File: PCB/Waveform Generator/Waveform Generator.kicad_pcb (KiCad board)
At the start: 4 copper layers, 80 x 104.1 mm, 141 parts, among them J1 Power input, J10 USART1_2, J12 Signal 2, J19 ADC_2, J2 RS485_1, J20 TIMER_1, J21 I2C1_1, J22 TIMER_2, J23 I2C1_2, J3 USB_B_Micro, J5 Signal 1, J6 SWD, J7 RS485_2, J8 USART1_1, J9 ADC_1, Q0 AO3401A, Q1 Q_NPN_BCE, Q2 Q_NPN_BCE, Q3 Q_PNP_BCE, Q4 Q_NPN_BCE, Q5 Q_NPN_BCE, Q6 Q_NPN_BCE, Q7 Q_NPN_BCE, Q8 Q_NPN_BCE, SW1 SW_SPDT, SW2 SW_SPDT, SW3 SW_SPDT, T0 5001, T1 5001, T2 5001, T3 5001, T4 5001, T5 5001, T6 5001, T7 5001, U1 STM32F427VITx, U10 USBLC6-2SC6, U11 USBLC6-2SC6, U2 MAX485EESAT, U3 USBLC6-2SC6, U4 OPA1602, U5 OPA1602, U6 USBLC6-2SC6, U7 USBLC6-2SC6, U8 LM335ADT, U9 USBLC6-2SC6, X1 25MHZ

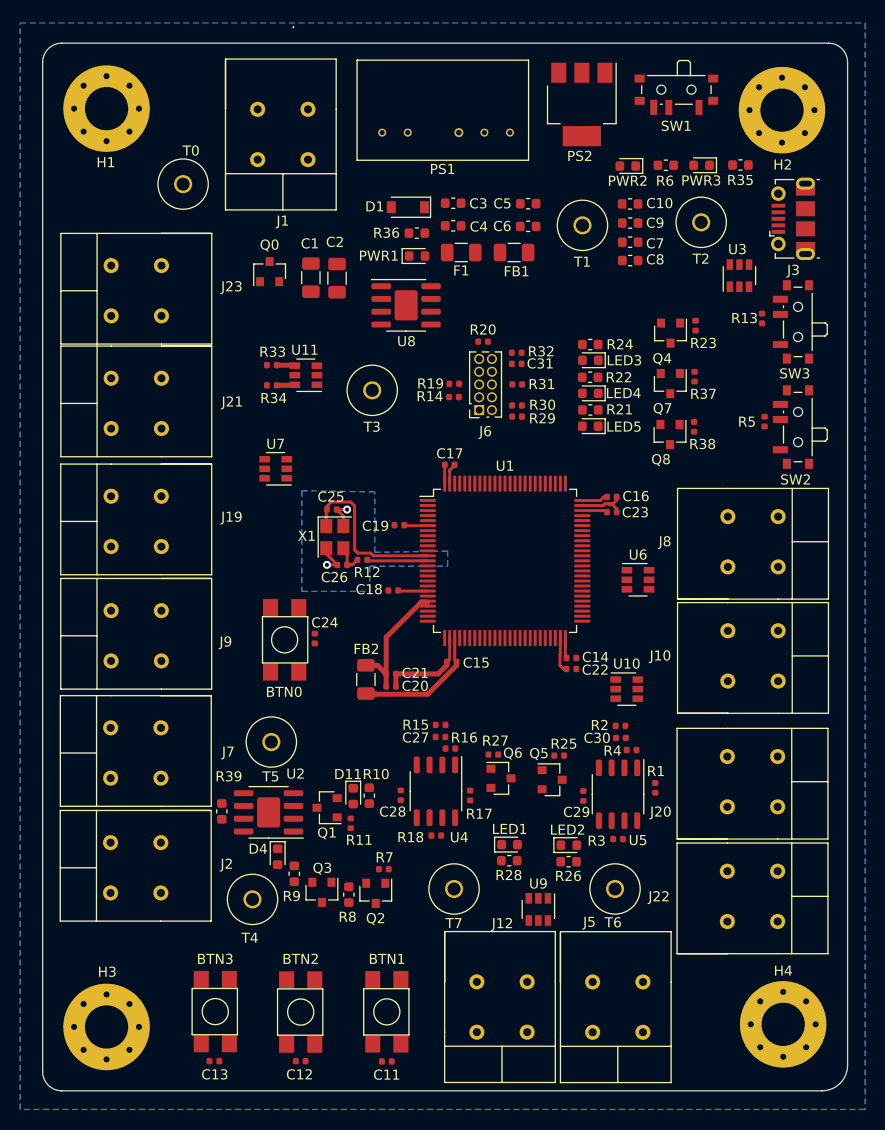
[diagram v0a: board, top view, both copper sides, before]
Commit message: Routing power
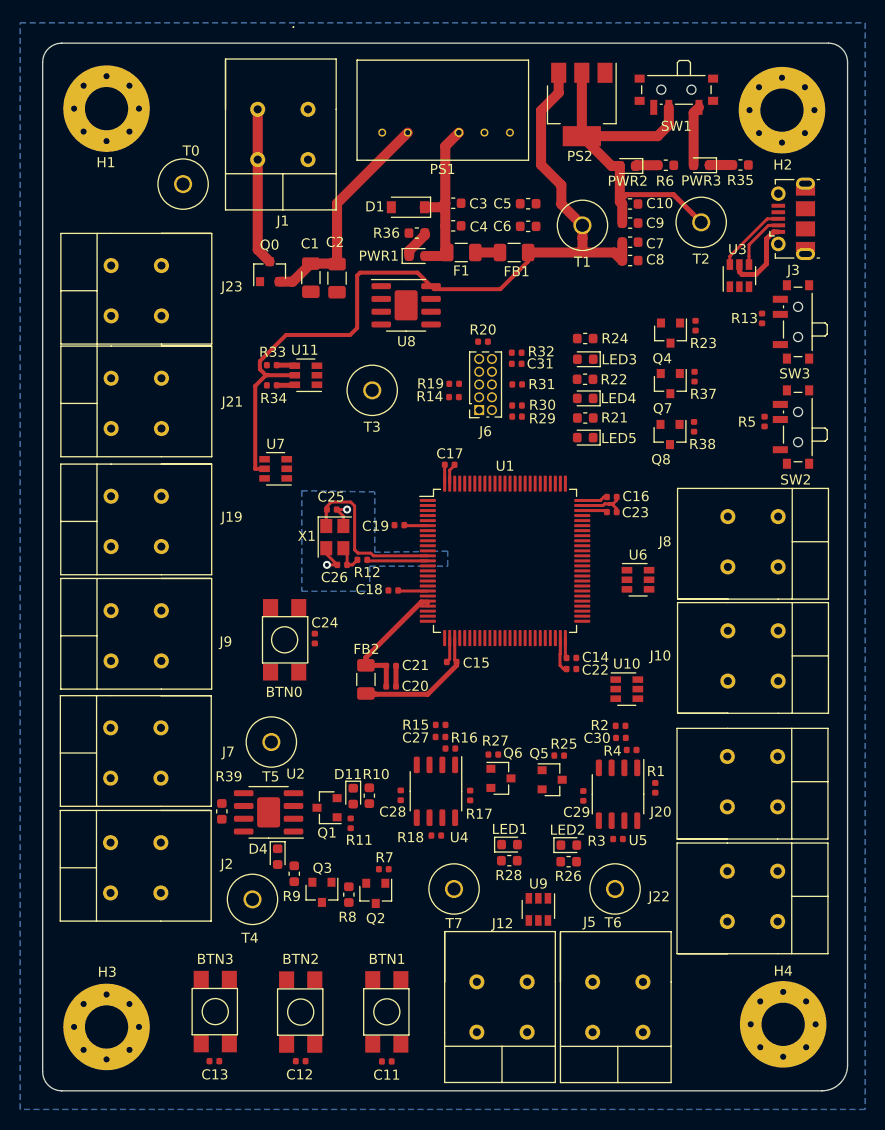
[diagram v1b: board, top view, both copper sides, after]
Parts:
- moved LED5 1.24 mm to (69.2, 48.1)
- moved R21 0.94 mm to (69.2, 46.1)
- moved C21 0.79 mm to (49.9, 70.8)
- moved R24 0.78 mm to (69.2, 38.2)
- moved LED4 0.71 mm to (69.2, 44.2)
- moved R22 0.54 mm to (69.2, 42.3)
- moved LED3 0.51 mm to (69.2, 40.3)
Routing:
- net +5V: track 0.00 -> 83.0 mm
- net Net-(C10-Pad1): track 0.00 -> 37.6 mm
- net Net-(C1-Pad1): track 0.00 -> 22.5 mm
- net Net-(C3-Pad1): track 0.00 -> 17.1 mm
- net VCC: track 0.00 -> 15.6 mm
- net VBUS: track 0.00 -> 7.89 mm
- net Net-(J3-Pad3): track 0.00 -> 7.19 mm
- net +3V3: track 24.9 -> 30.9 mm
- net Net-(J3-Pad2): track 0.00 -> 5.68 mm
- net GND: track 27.0 -> 22.0 mm
- net Net-(PWR1-Pad1): track 0.00 -> 2.92 mm
- net Net-(F1-Pad1): track 0.00 -> 2.45 mm
- net Net-(PWR3-Pad1): track 0.00 -> 2.30 mm
- net Net-(PWR2-Pad1): track 0.00 -> 2.24 mm

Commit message: Working on PCB tracks
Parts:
- moved Q7 5.30 mm to (77.7, 48.0)
- moved R37 5.27 mm to (80.3, 47.3)
- moved R38 5.04 mm to (80.2, 42.0)
- moved Q8 4.99 mm to (77.7, 42.8)
- moved U6 1.83 mm to (74.9, 64.0)
- moved T3 1.57 mm to (48.7, 42.0)
- moved C15 1.06 mm to (55.2, 71.2)
- moved H3 0.18 mm to (21.6, 106.5)
- moved J8 0.07 mm to (83.2, 58.4)
- turned LED2 to 180 degrees
- turned R31 to 180 degrees
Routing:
- net BTN3_Input: track 0.00 -> 69.0 mm, vias 0 -> 2
- net BTN2_Input: track 0.00 -> 65.7 mm, vias 0 -> 2
- net BTN1_Input: track 0.00 -> 58.2 mm, vias 0 -> 2
- net +5V: track 83.0 -> 33.7 mm, vias 0 -> 1
- net MAX485_PWR: track 0.00 -> 38.8 mm, vias 0 -> 2
- net ADC2_IN0: track 0.00 -> 33.0 mm, vias 0 -> 2
- net LED3: track 0.00 -> 31.5 mm
- net NRST: track 0.00 -> 28.9 mm
- net ADC1_IN1: track 0.00 -> 27.9 mm, vias 0 -> 2
- net USART2_RX: track 0.00 -> 27.1 mm, vias 0 -> 2
- net Net-(J7-Pad1): track 0.00 -> 26.8 mm
- net Net-(J22-Pad1): track 0.00 -> 26.4 mm
- net LED1: track 0.00 -> 25.6 mm, vias 0 -> 2
- net LED4: track 0.00 -> 25.4 mm
- net Net-(J2-Pad2): track 0.00 -> 23.4 mm
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- removed copper zone on In2.Cu, net +3V3
- removed copper zone on B.Cu, net GND

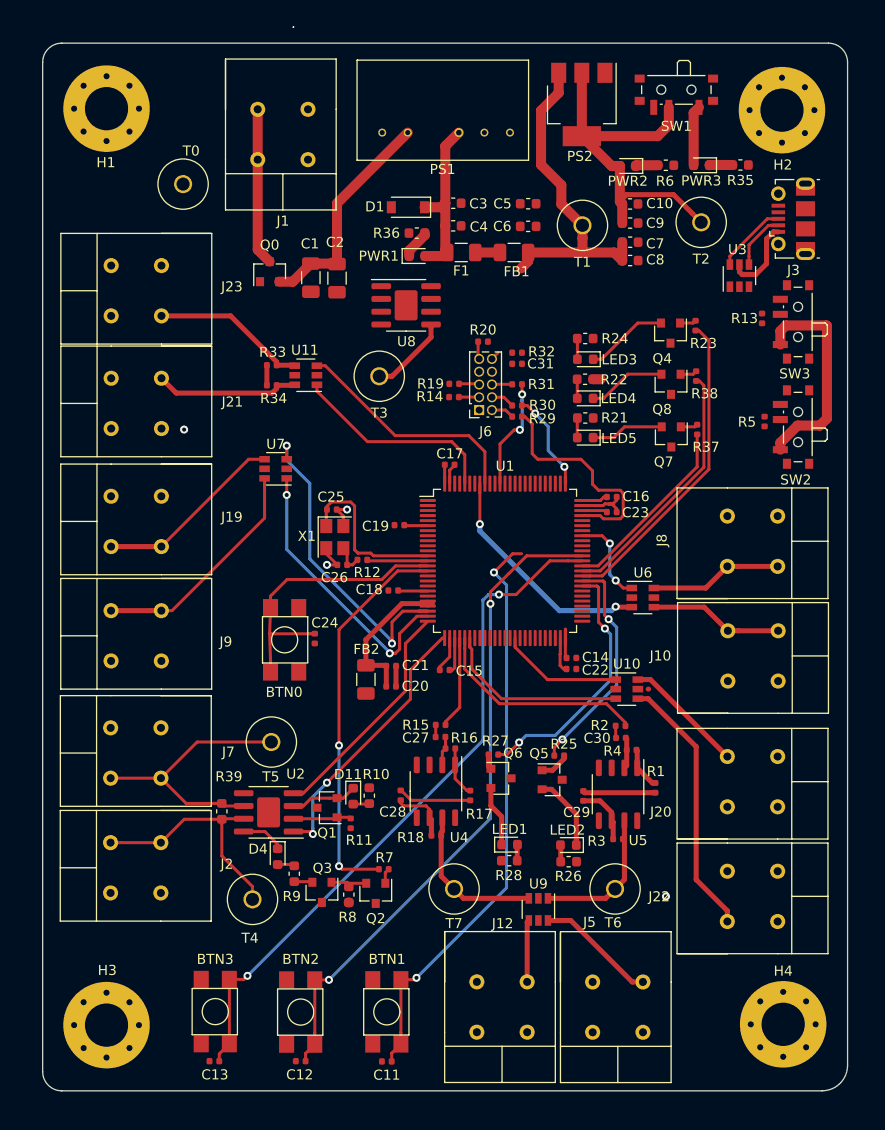
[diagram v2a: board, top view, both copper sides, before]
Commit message: Busy with ground planes
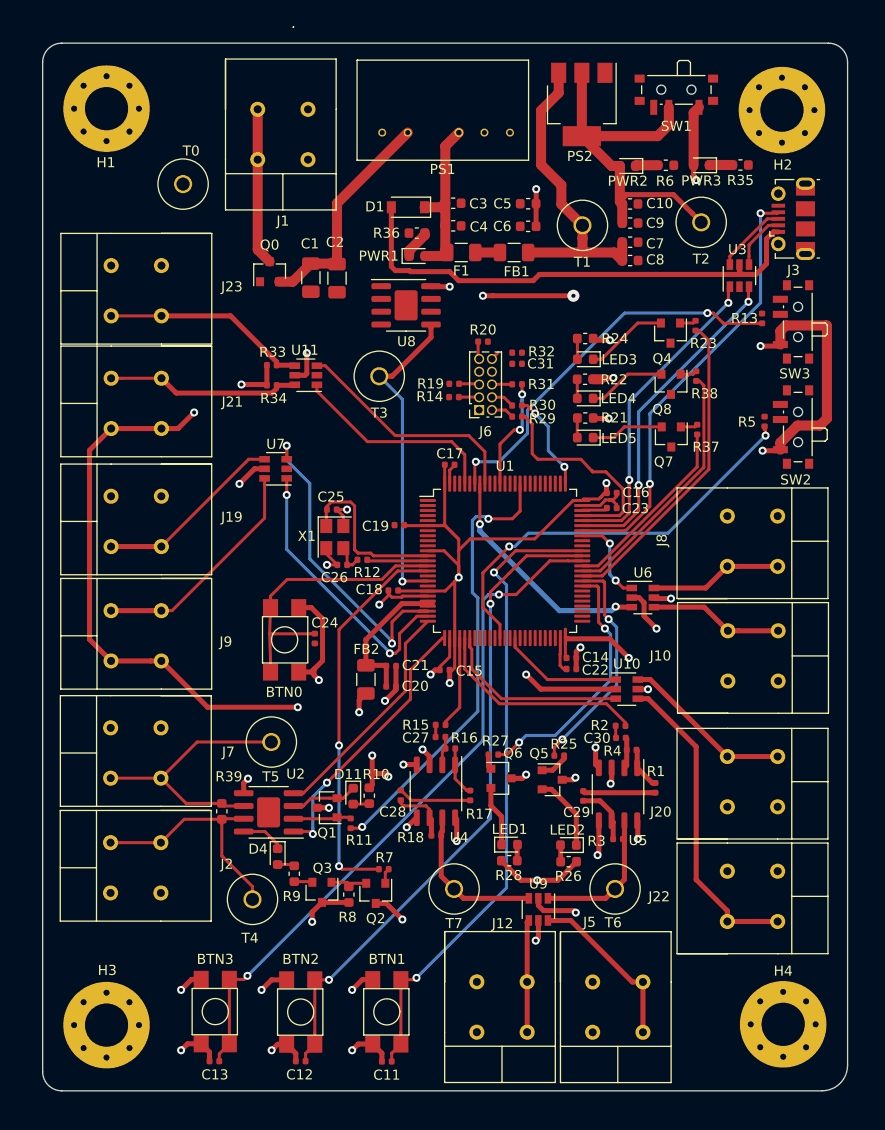
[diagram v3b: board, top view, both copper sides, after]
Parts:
- moved C16 0.40 mm to (71.8, 53.6)
- moved C23 0.40 mm to (71.8, 55.1)
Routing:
- net +3V3: track 46.9 -> 482.6 mm, vias 1 -> 19
- net +5V: track 33.7 -> 238.2 mm, vias 1 -> 9
- net -5V: track 0.00 -> 128.0 mm, vias 0 -> 3
- net GND: track 23.1 -> 102.4 mm, vias 2 -> 25
- net USART2_RTS: track 0.00 -> 44.7 mm, vias 0 -> 2
- net USB_ID: track 0.00 -> 43.2 mm, vias 0 -> 2
- net VBUS: track 7.89 -> 50.1 mm
- net BOOT1: track 0.00 -> 42.0 mm, vias 0 -> 2
- net BOOT0: track 0.00 -> 38.6 mm, vias 0 -> 2
- net USB_D-: track 0.00 -> 33.0 mm, vias 0 -> 2
- net USB_D+: track 0.00 -> 32.5 mm, vias 0 -> 2
- net TEMP_SENSE: track 8.02 -> 31.9 mm, vias 0 -> 1
- net BTN1_Input: track 58.2 -> 64.4 mm
- net Net-(J5-Pad1): track 12.0 -> 17.0 mm
- net Net-(J21-Pad2): track 14.4 -> 19.4 mm
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- added copper zone on In2.Cu, net +3V3

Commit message: Benchmark, looks if the majority of the work is complete
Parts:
- moved C23 1.62 mm to (71.0, 53.7)
- moved C16 1.29 mm to (71.0, 52.6)
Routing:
- net GND: track 102.4 -> 190.5 mm, vias 25 -> 49
- net NRST: track 28.9 -> 62.1 mm, vias 0 -> 2
- net +3V3: track 482.6 -> 478.9 mm, vias 19 -> 18
- net Net-(LED4-Pad1): track 7.69 -> 10.3 mm
- net Net-(LED3-Pad1): track 8.22 -> 10.3 mm
- net Net-(R5-Pad1): track 0.00 -> 1.69 mm
- net Net-(J6-Pad10): track 0.88 -> 2.27 mm
- net SWDIO: track 22.2 -> 22.7 mm

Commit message: Monday morning grind
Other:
- board text added: "Waveform Generator V1 Nanodyn Systems"
- board text removed: "Waveform Generator v1 Nanodyn Systems"
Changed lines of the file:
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@@
     (32 B.Adhes user)
     (33 F.Adhes user)
-    (34 B.Paste user)
+    (34 B.Paste user hide)
     (35 F.Paste user)
     (36 B.SilkS user)
@@
     (tags capacitor)
     (attr smd)
-    (fp_text reference C1 (at -3.37 0.09 180) (layer F.SilkS)
+    (fp_text reference C1 (at -3 0 180) (layer F.SilkS)
       (effects (font (size 1 1) (thickness 0.15)))
     )
@@
     (tags capacitor)
     (attr smd)
-    (fp_text reference C2 (at 3.57 -0.19 180) (layer F.SilkS)
+    (fp_text reference C2 (at 3.05 0 180) (layer F.SilkS)
       (effects (font (size 1 1) (thickness 0.15)))
     )
@@
     (tags capacitor)
     (attr smd)
-    (fp_text reference C31 (at -2.35 0) (layer F.SilkS)
+    (fp_text reference C31 (at -2.4 -0.04) (layer F.SilkS)
       (effects (font (size 1 1) (thickness 0.15)))
     )
@@
     (tags SOT-23)
     (attr smd)
-    (fp_text reference Q0 (at 2.65 0 180) (layer F.SilkS)
+    (fp_text reference Q0 (at 2.5 0.1 180) (layer F.SilkS)
       (effects (font (size 1 1) (thickness 0.15)))
     )
@@
     (tags resistor)
     (attr smd)
-    (fp_text reference R13 (at 0 1.75 180) (layer F.SilkS)
+    (fp_text reference R13 (at 0.05 1.95 180) (layer F.SilkS)
       (effects (font (size 1 1) (thickness 0.15)))
     )
@@
     (tags resistor)
     (attr smd)
-    (fp_text reference R31 (at -2.415 0) (layer F.SilkS)
+    (fp_text reference R31 (at -2.5 0) (layer F.SilkS)
       (effects (font (size 1 1) (thickness 0.15)))
     )
@@
     (tags resistor)
     (attr smd)
-    (fp_text reference R14 (at 2.4 0.05) (layer F.SilkS)
+    (fp_text reference R14 (at 2.425 -0.03) (layer F.SilkS)
       (effects (font (size 1 1) (thickness 0.15)))
     )
@@
     (tags resistor)
     (attr smd)
-    (fp_text reference R19 (at 2.35 0) (layer F.SilkS)
+    (fp_text reference R19 (at 2.445 -0.05) (layer F.SilkS)
       (effects (font (size 1 1) (thickness 0.15)))
     )
@@
   (gr_arc (start 17.145 111.125) (end 15.24 111.125) (angle -90) (layer Edge.Cuts) (width 0.05))
   (gr_arc (start 92.71 110.49) (end 92.71 113.03) (angle -90) (layer Edge.Cuts) (width 0.05))
-  (gr_text "Waveform Generator v1\nNanodyn Systems" (at 60.65 79.1) (layer B.SilkS)
+  (gr_text "Waveform Generator V1\nNanodyn Systems" (at 40.2 101.9) (layer B.SilkS)
     (effects (font (size 1.5 1.5) (thickness 0.3)) (justify mirror))
   )

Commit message: Almost finished with the PCB design
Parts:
- removed T6: 5001, Extra Components:5001 Test Point
- added ?: , , F.Cu at (-9.10, 4.50)
- added ?: , , F.Cu at (25.4, 26.9)
- added DAC_OUT_2: 5001, Extra Components:5001 Test Point, F.Cu at (72.1, 93.0)
- moved H4 1.54 mm to (88.6, 108.0)
- moved H3 0.98 mm to (21.8, 107.4)
- renumbered T2 to 3V3, T1 to 5V, T7 to DAC_OUT_1, T0 to GND, T5 to RS485_A, T4 to RS485_B, T3 to TEMP_SENSE
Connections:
- U1 pad 24: ADC1_IN1 -> GND
- U7 pad 1: ADC1_IN1 -> GND
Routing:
- net GND: track 190.5 -> 224.7 mm, vias 49 -> 106
- net ADC1_IN1: track 27.9 -> 0.00 mm, vias 2 -> 0
- net Net-(R13-Pad1): track 0.00 -> 1.86 mm
- net USART2_RTS: vias 2 -> 3
- net USART1_RX: vias 2 -> 3
- net +3V3: vias 18 -> 19
- net (no net): vias 0 -> 54
- added copper zone on F.Cu, net GND
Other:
- board size 80 x 104.1 mm -> 80 x 105.2 mm
- board text added: "3V3"
- board text added: "5V"
- board text added: "ADC1_IN1"
- board text added: "ADC2_IN0"
- board text added: "DAC_OUT_1"
- board text added: "DAC_OUT_2"
- board text added: "GND"
- board text added: "I2C1SCL"
- board text added: "I2C1_SDA"
- board text added: "NC"
- board text added: "RS485_A"
- board text added: "RS485_B"
- board text added: "TIM1_CH1"
- board text added: "TIM3_CH1"
- board text added: "USART1_RX"
- board text added: "USART1_TX"

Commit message: Almost done
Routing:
- net GND: vias 106 -> 229
- net (no net): vias 54 -> 0
- added copper zone on B.Cu, net GND

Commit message: Benchmark, final PCB layout
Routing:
- net GND: track 224.7 -> 218.4 mm
- net +3V3: track 478.9 -> 477.3 mm, vias 19 -> 22
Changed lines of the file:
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@@
     (thickness 1.6)
     (drawings 41)
-    (tracks 1289)
+    (tracks 1288)
     (zones 0)
     (modules 143)
@@
     (31 B.Cu signal)
     (32 B.Adhes user)
-    (33 F.Adhes user)
+    (33 F.Adhes user hide)
     (34 B.Paste user hide)
     (35 F.Paste user)
@@
     (descr "Ultraminiature Surface Mount Slide Switch, right-angle, https://www.ckswitches.com/media/1424/pcm.pdf")
     (attr smd)
-    (fp_text reference SW1 (at 0 -3.3) (layer F.SilkS)
+    (fp_text reference SW1 (at 0.292 -3.247) (layer F.SilkS)
       (effects (font (size 1 1) (thickness 0.15)))
     )
@@
     (effects (font (size 1.5 1.5) (thickness 0.3)) (justify mirror))
   )
+  (via (at 79.95 19.82) (size 1) (drill 0.4) (layers F.Cu B.Cu) (net 9))
+  (via (at 79.95 16.78) (size 1) (drill 0.4) (layers F.Cu B.Cu) (net 9))
+  (via (at 79.95 17.79) (size 1) (drill 0.4) (layers F.Cu B.Cu) (net 9))
   (via (at 26.5 44.5) (size 0.8) (drill 0.4) (layers F.Cu B.Cu) (net 2) (status 40000))
   (via (at 23.25 44.5) (size 0.8) (drill 0.4) (layers F.Cu B.Cu) (net 2) (status 40000))
@@
   (segment (start 74.427 24.8865) (end 74.4145 24.874) (width 0.5) (layer F.Cu) (net 2))
   (segment (start 74.427 30.5) (end 74.427 24.8865) (width 0.5) (layer F.Cu) (net 2))
-  (segment (start 79.820501 23.350001) (end 83.512499 23.350001) (width 0.5) (layer F.Cu) (net 2))
   (segment (start 85.3875 21.475) (end 85.3875 21) (width 0.5) (layer F.Cu) (net 2))
-  (segment (start 77.9725 21.502) (end 79.820501 23.350001) (width 0.5) (layer F.Cu) (net 2))
   (segment (start 83.512499 23.350001) (end 85.3875 21.475) (width 0.5) (layer F.Cu) (net 2))
   (segment (start 77.9725 21.027) (end 77.9725 21.502) (width 0.5) (layer F.Cu) (net 2))
@@
   (segment (start 56.2 68.825) (end 56.2 68.025) (width 0.3) (layer F.Cu) (net 9))
   (segment (start 55.685 71.2) (end 55.98 71.2) (width 0.3) (layer F.Cu) (net 9))
-  (via (at 80.2 22.5) (size 0.8) (drill 0.4) (layers F.Cu B.Cu) (net 9))
-  (segment (start 79.9475 21.027) (end 79.9475 22.2475) (width 0.5) (layer F.Cu) (net 9))
-  (segment (start 79.9475 22.2475) (end 80.2 22.5) (width 0.5) (layer F.Cu) (net 9))
+  (via (at 79.95 18.8) (size 1) (drill 0.4) (layers F.Cu B.Cu) (net 9))
   (via (at 86.6 39) (size 0.8) (drill 0.4) (layers F.Cu B.Cu) (net 9))
   (segment (start 80.2 22.5) (end 86.6 28.9) (width 0.5) (layer In2.Cu) (net 9))
